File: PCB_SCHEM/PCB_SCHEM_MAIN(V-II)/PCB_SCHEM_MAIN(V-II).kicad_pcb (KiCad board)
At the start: 2 copper layers, 20 parts, among them J1 USB_C_Receptacle_USB2.0_14P, U1 RP2040, U2 TPS61291DRVR, U3 LSM6DS3, U4 MX25L3233FM1, U5 MX25L3233FM1, Y1 Crystal_GND24

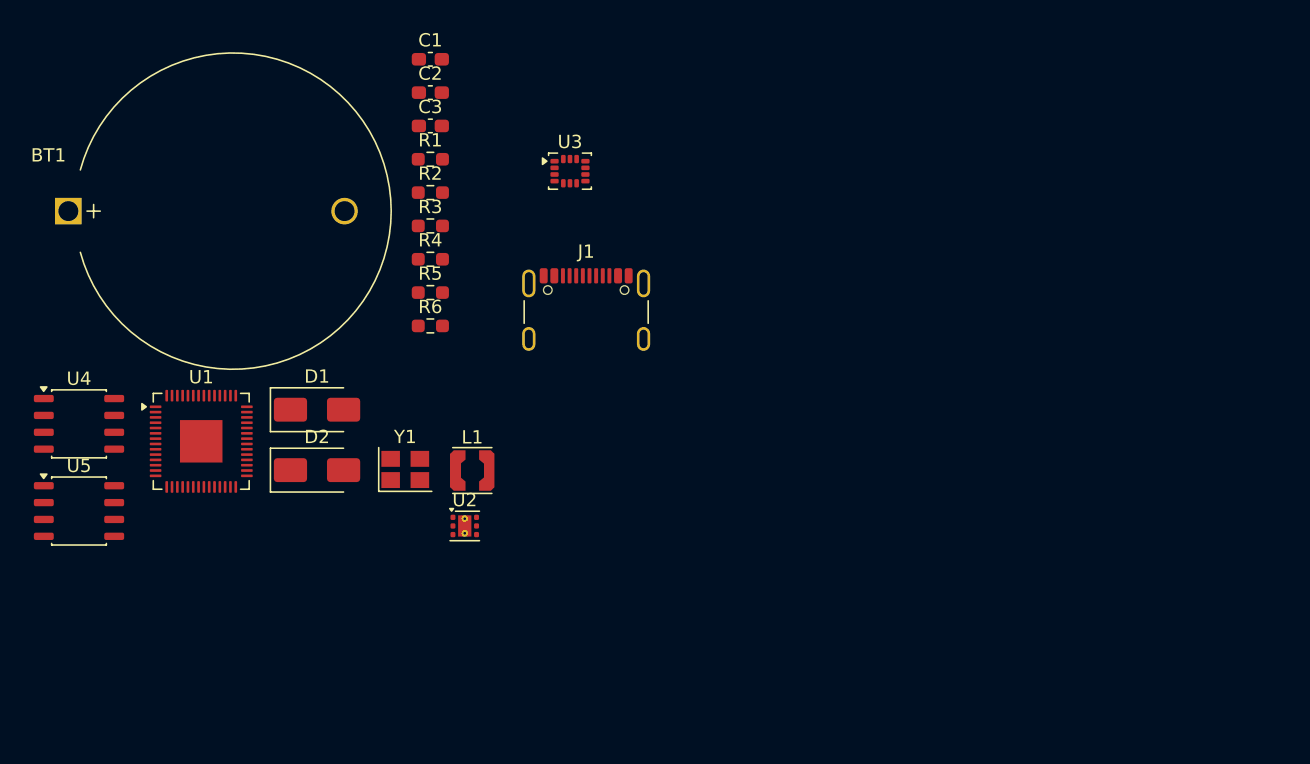
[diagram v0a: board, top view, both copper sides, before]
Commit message: PCB design and schematic fully completed. No further changes, maybe minor trace shifts at best. PCB step file is exported to Fusion, enclousre yet to be designed.
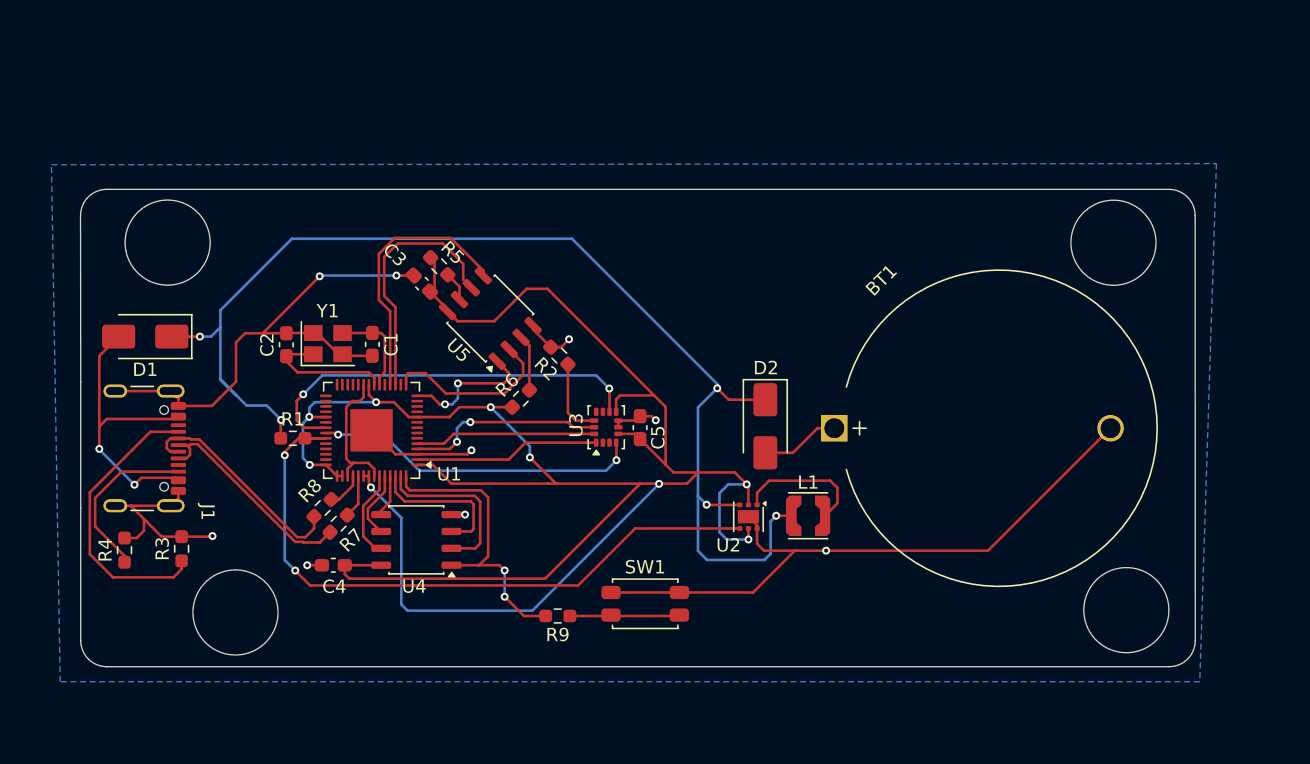
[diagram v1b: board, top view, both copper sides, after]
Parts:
- added C4: 100nf, Capacitor_SMD:C_0603_1608Metric_Pad1.08x0.95mm_HandSolder, F.Cu at (117.2, 110.2)
- added C5: 100nf, Capacitor_SMD:C_0603_1608Metric_Pad1.08x0.95mm_HandSolder, F.Cu at (140.3, 99.8)
- added R7: 27, Resistor_SMD:R_0603_1608Metric_Pad0.98x0.95mm_HandSolder, F.Cu at (117.6, 107.0)
- added R8: 27, Resistor_SMD:R_0603_1608Metric_Pad0.98x0.95mm_HandSolder, F.Cu at (116.4, 105.9)
- added R9: 1K, Resistor_SMD:R_0603_1608Metric_Pad0.98x0.95mm_HandSolder, F.Cu at (134.2, 114.0)
- added SW1: SW_Push, Button_Switch_SMD:SW_SPST_EVQP2_MiddlePushTravel_H2.5mm, F.Cu at (140.7, 113.1)
- U2: footprint Package_SON:WSON-6-1EP_2x2mm_P0.65mm_EP1x1.6mm_ThermalVias -> Package_SON:WSON-6-1EP_2x2mm_P0.65mm_EP1x1.6mm
- moved BT1 60.0 mm to (155.0, 99.9)
- moved J1 35.6 mm to (101.9, 101.4), turned to -90 degrees
- moved U5 34.2 mm to (129.1, 91.6), turned to 135 degrees
- moved D2 33.9 mm to (149.8, 99.7), turned to -90 degrees
- moved R4 31.8 mm to (101.5, 109.0), turned to 90 degrees
- moved R3 30.7 mm to (105.8, 108.9), turned to 90 degrees
- moved U4 26.9 mm to (123.5, 108.3), turned to 180 degrees
- moved L1 25.5 mm to (153.0, 106.4)
- moved R1 23.4 mm to (114.2, 100.6)
- moved C1 21.9 mm to (120.2, 93.5), turned to -90 degrees
- moved C2 21.9 mm to (113.7, 93.6), turned to 90 degrees
- moved U2 21.4 mm to (148.5, 106.5), turned to -90 degrees
- moved U3 19.5 mm to (137.8, 99.8), turned to 90 degrees
- moved R2 15.7 mm to (134.3, 94.4), turned to 135 degrees
- moved D1 14.1 mm to (103.1, 93.0), turned to 180 degrees
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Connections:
- J1 pad A6: Net-(U1-USB_DP) -> /D+
- J1 pad A7: Net-(U1-USB_DM) -> /D-
- J1 pad B6: Net-(U1-USB_DP) -> /D+
- J1 pad B7: Net-(U1-USB_DM) -> /D-
- U1 pad 46: Net-(U1-USB_DM) -> /MCU_DN
- U1 pad 47: Net-(U1-USB_DP) -> /MCU_DP
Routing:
- net /3.3V: track 0.00 -> 175.4 mm, vias 0 -> 9
- net GND: track 0.00 -> 119.5 mm, vias 0 -> 9
- net /VIN: track 0.00 -> 93.1 mm, vias 0 -> 5
- net Net-(U1-GPIO25): track 0.00 -> 50.1 mm, vias 0 -> 2
- net Net-(U1-GPIO23): track 0.00 -> 30.4 mm, vias 0 -> 2
- net Net-(U1-GPIO24): track 0.00 -> 24.7 mm, vias 0 -> 2
- net Net-(D1-A): track 0.00 -> 23.4 mm, vias 0 -> 2
- net /CS: track 0.00 -> 22.6 mm, vias 0 -> 2
- net Net-(J1-CC1): track 0.00 -> 21.7 mm
- net Net-(U1-GPIO15): track 0.00 -> 20.0 mm
- net Net-(U1-GPIO14): track 0.00 -> 19.0 mm
- net /D+: track 0.00 -> 17.3 mm
- net /D-: track 0.00 -> 16.9 mm
- net Net-(U1-GPIO2): track 0.00 -> 14.9 mm, vias 0 -> 2
- net Net-(U1-GPIO0): track 0.00 -> 14.0 mm
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- added copper zone on B.Cu, net GND
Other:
- board outline added: 84 x 36 mm

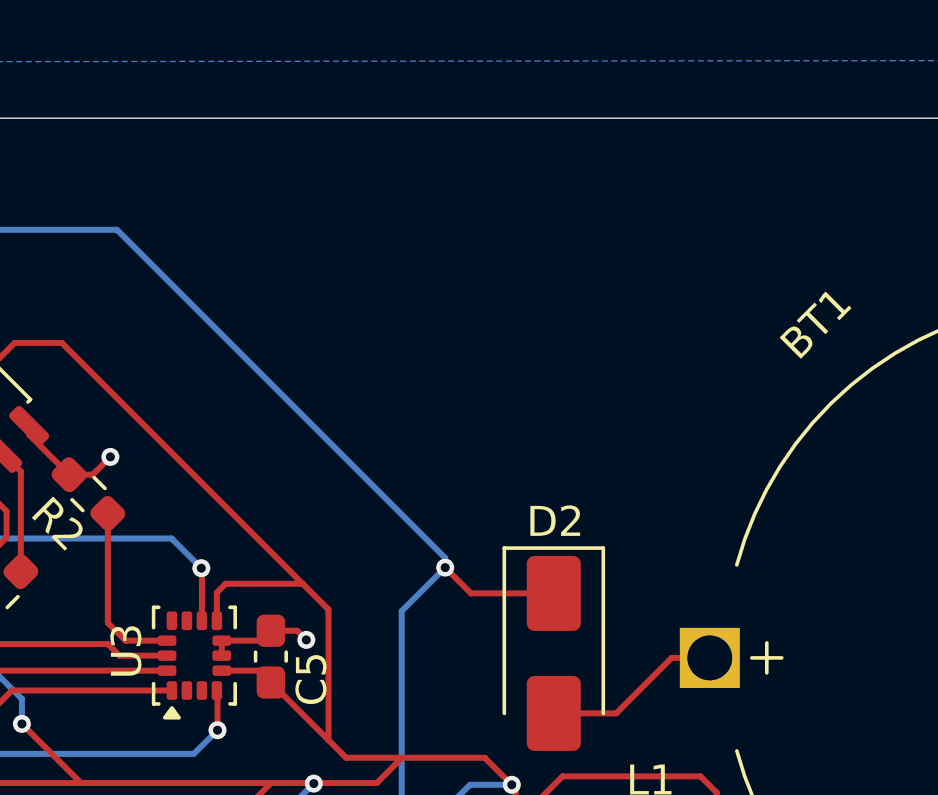
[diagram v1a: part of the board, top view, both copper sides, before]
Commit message: Added singature trademark to PCB design
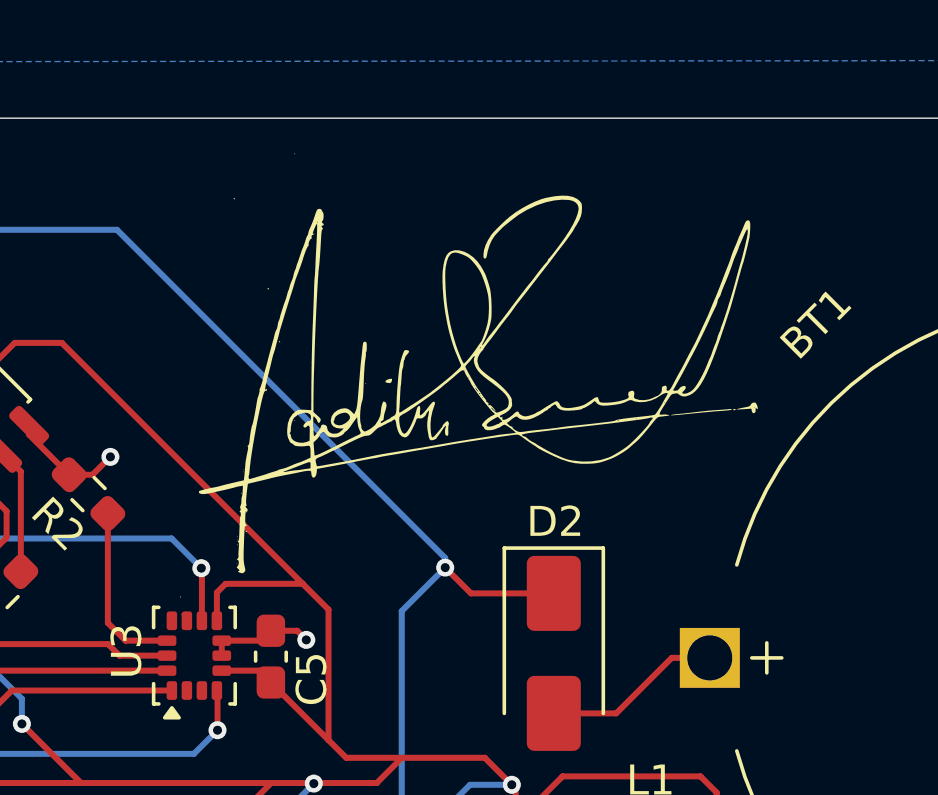
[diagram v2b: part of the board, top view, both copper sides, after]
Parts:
- added G***: LOGO, KiCAD projects:SIgnature_B_16.0mm_20.0mm, F.Cu at (147.2, 91.1)

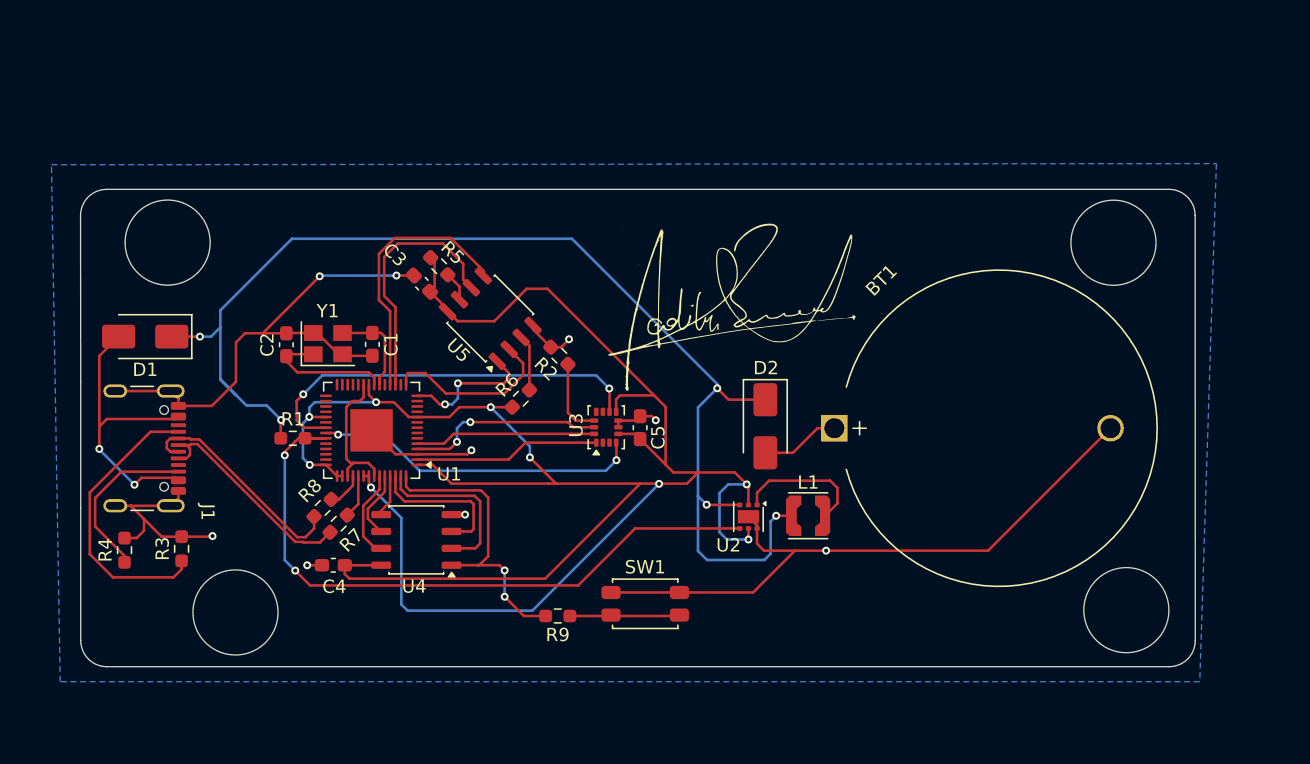
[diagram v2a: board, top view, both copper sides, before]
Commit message: Added Teardrops, Reference silkscreen text and trademark symbol. Used proper track widths and fixed fatal overhaeting errors.
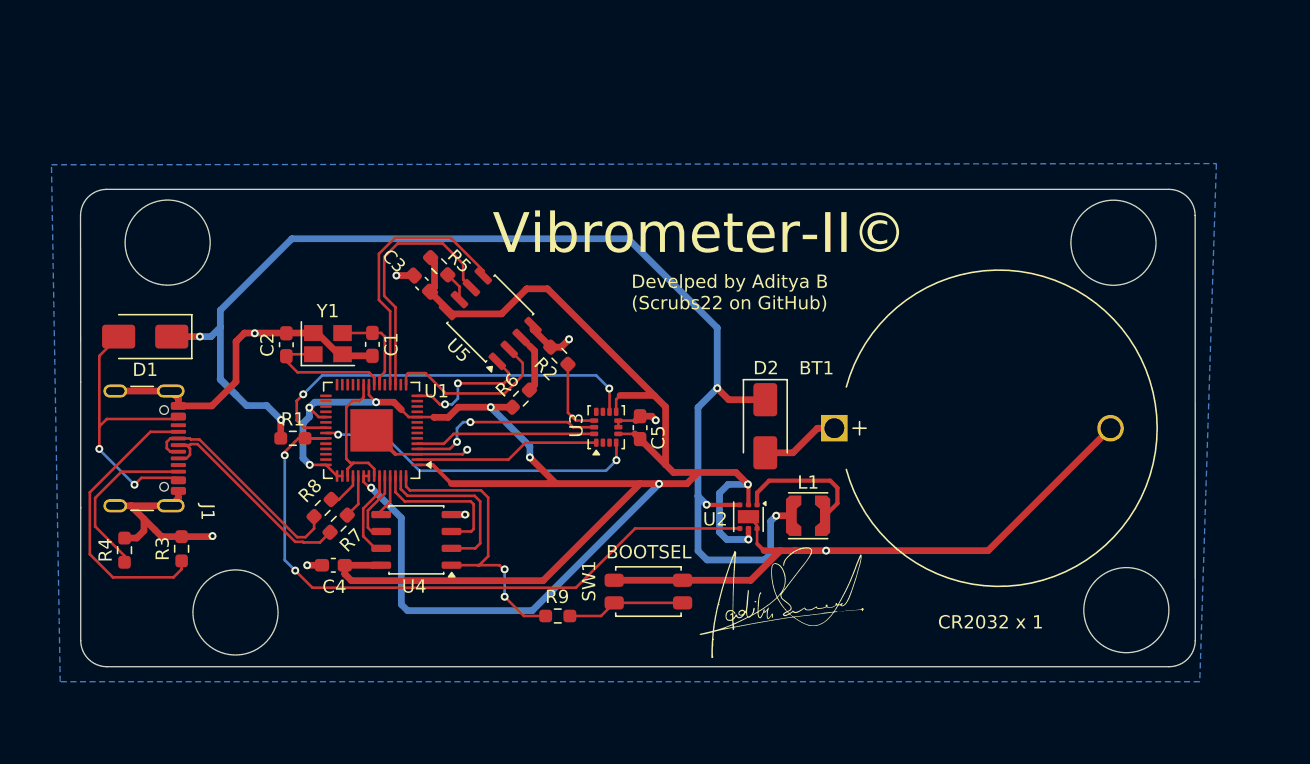
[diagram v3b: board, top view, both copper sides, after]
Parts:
- removed the G*** at (147.2, 91.1)
- added G***: LOGO, KiCAD projects:Sign_10.13.3mm, F.Cu at (151.2, 113.3)
- added G***: LOGO, KiCAD projects:Sign_Back_20x20.3, B.Cu at (134.6, 95.6)
- moved SW1 0.95 mm to (141.0, 112.2)
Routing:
- net GND: track 119.5 -> 105.6 mm
- net /VIN: track 93.1 -> 95.5 mm
- net /3.3V: track 175.4 -> 176.0 mm
- net Net-(R9-Pad1): track 8.28 -> 8.90 mm
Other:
- board text added: "BOOTSEL"
- board text added: "CR2032 x 1"
- board text added: "Develped by Aditya B (Scrubs22 on GitHub)"
- board text added: "Vibrometer-II©"

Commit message: Fixed major LSM6DS3 sleep function wiring error and furnished traces. Also added track to track teardrops. 3D view pictures also added.
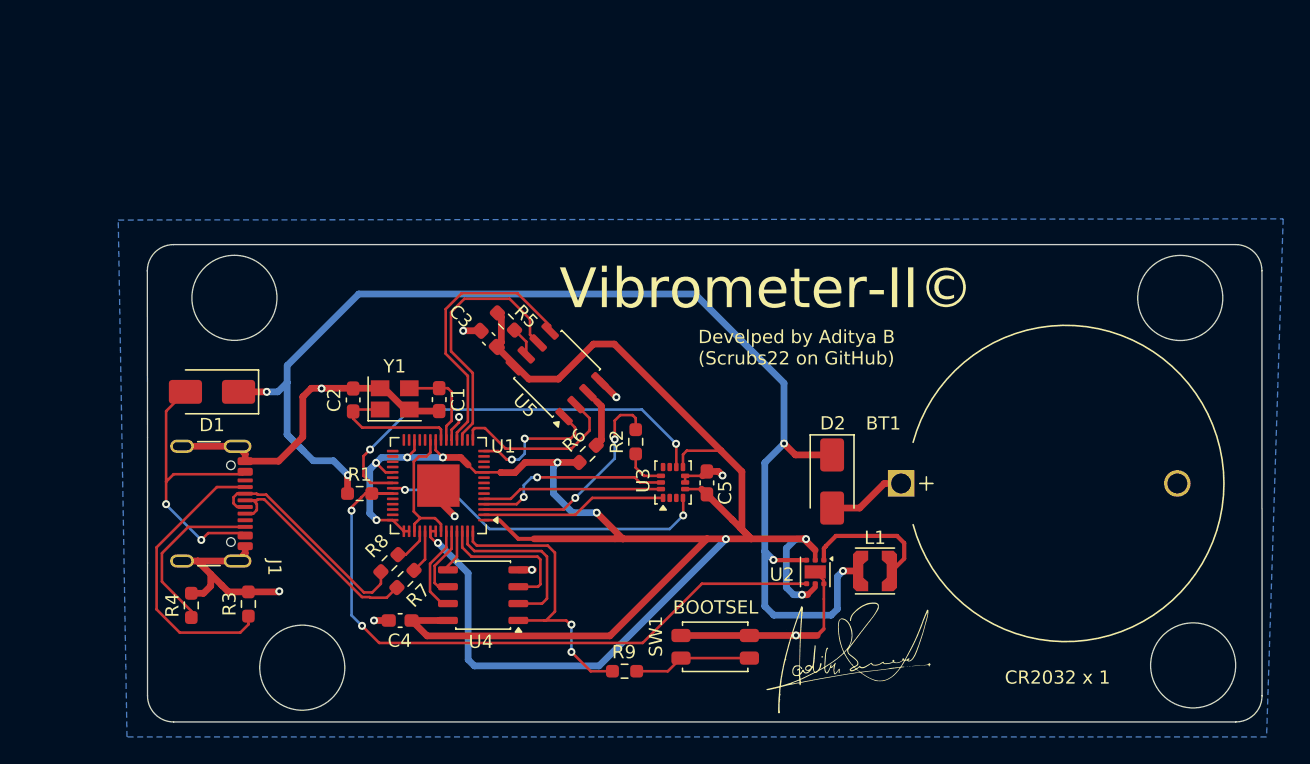
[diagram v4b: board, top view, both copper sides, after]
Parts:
- moved G*** 10.4 mm to (140.0, 104.5)
- moved R2 8.66 mm to (140.0, 100.9), turned to 90 degrees
- moved R9 6.53 mm to (139.2, 118.2)
- moved C1 6.53 mm to (125.2, 97.7)
- moved R3 6.53 mm to (110.9, 113.1)
- moved BT1 6.53 mm to (160.0, 104.0)
- moved C2 6.53 mm to (118.7, 97.7)
- moved C3 6.53 mm to (128.9, 93.1)
- moved C4 6.53 mm to (122.3, 114.3), turned to 180 degrees
- moved C5 6.53 mm to (145.4, 104.0)
- moved D1 6.53 mm to (108.1, 97.1)
- moved D2 6.53 mm to (154.8, 103.9)
- moved G*** 6.53 mm to (156.2, 117.5)
- moved J1 6.53 mm to (106.9, 105.5)
- moved L1 6.53 mm to (158.0, 110.6)
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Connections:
- C4 pad 1: GND -> /3.3V
- C4 pad 2: /3.3V -> GND
- R2 pad 2: GND -> Net-(U1-GPIO1)
- U1 pad 19: unconnected-(U1-TESTEN-Pad19) -> GND
- U1 pad 26: unconnected-(U1-RUN-Pad26) -> /3.3V
- U1 pad 3: GND -> Net-(U1-GPIO1)
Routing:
- net GND: track 105.6 -> 69.4 mm, vias 9 -> 10
- net Net-(U1-GPIO1): track 0.00 -> 17.0 mm, vias 0 -> 2
- net Net-(U3-CS): track 5.87 -> 3.19 mm
- net /3.3V: track 176.0 -> 178.3 mm, vias 9 -> 10
- net Net-(U1-GPIO23): track 30.4 -> 31.7 mm
- net Net-(U1-GPIO15): track 20.0 -> 20.7 mm
- net Net-(U1-GPIO14): track 19.0 -> 19.7 mm
